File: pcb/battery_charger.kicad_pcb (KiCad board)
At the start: 2 copper layers, 36.2 x 24.2 mm, 20 parts, among them J1 USB_B_Micro, U1 TP4056, U2 DW01A, U3 FS8205A

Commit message: Correcciones generales al pcb
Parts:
- moved C1 0.32 mm to (123.3, 124.8), turned to 0 degrees
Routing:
- net GND: track 97.6 -> 95.7 mm
- net +5V: track 51.4 -> 50.6 mm
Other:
- board text added: "1"
- board text added: "Rev. 1.0"
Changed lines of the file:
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@@
   (general
     (thickness 1.6)
-    (drawings 8)
-    (tracks 145)
+    (drawings 12)
+    (tracks 144)
     (zones 0)
     (modules 20)
@@
   )
   (setup
-    (last_trace_width 0.25)
+    (last_trace_width 0.5)
     (user_trace_width 0.25)
     (user_trace_width 0.5)
@@
   )
   (module Capacitor_SMD:C_0805_2012Metric (layer F.Cu)
-    (at 123.25 125.0625 270)
+    (at 123.3125 124.75)
     (descr "Capacitor SMD 0805 (2012 Metric), square (rectangular) end terminal, IPC_7351 nominal, (Body size source: https://docs.google.com/spreadsheets/d/1BsfQQcO9C6DZCsRaXUlFlo91Tg2WpOkGARC1WS5S8t0/edit?usp=sharing), generated with kicad-footprint-generator")
     (tags capacitor)
     (attr smd)
-    (fp_text reference C1 (at -0.0625 -2 180) (layer F.SilkS)
-      (effects (font (size 1 1) (thickness 0.15)))
-    )
-    (fp_text value 0.1uF (at 0 1.65 90) (layer F.Fab)
-      (effects (font (size 1 1) (thickness 0.15)))
-    )
-    (fp_text user %R (at 0 0 90) (layer F.Fab)
+    (fp_text reference C1 (at 0.1875 -1.75) (layer F.SilkS)
+      (effects (font (size 1 1) (thickness 0.15)))
+    )
+    (fp_text value 0.1uF (at 0 1.65) (layer F.Fab)
+      (effects (font (size 1 1) (thickness 0.15)))
+    )
+    (fp_line (start -1 0.6) (end -1 -0.6) (layer F.Fab) (width 0.1))
+    (fp_line (start -1 -0.6) (end 1 -0.6) (layer F.Fab) (width 0.1))
+    (fp_line (start 1 -0.6) (end 1 0.6) (layer F.Fab) (width 0.1))
+    (fp_line (start 1 0.6) (end -1 0.6) (layer F.Fab) (width 0.1))
+    (fp_line (start -0.258578 -0.71) (end 0.258578 -0.71) (layer F.SilkS) (width 0.12))
+    (fp_line (start -0.258578 0.71) (end 0.258578 0.71) (layer F.SilkS) (width 0.12))
+    (fp_line (start -1.68 0.95) (end -1.68 -0.95) (layer F.CrtYd) (width 0.05))
+    (fp_line (start -1.68 -0.95) (end 1.68 -0.95) (layer F.CrtYd) (width 0.05))
+    (fp_line (start 1.68 -0.95) (end 1.68 0.95) (layer F.CrtYd) (width 0.05))
+    (fp_line (start 1.68 0.95) (end -1.68 0.95) (layer F.CrtYd) (width 0.05))
+    (fp_text user %R (at 0 0) (layer F.Fab)
       (effects (font (size 0.5 0.5) (thickness 0.08)))
     )
-    (fp_line (start 1.68 0.95) (end -1.68 0.95) (layer F.CrtYd) (width 0.05))
-    (fp_line (start 1.68 -0.95) (end 1.68 0.95) (layer F.CrtYd) (width 0.05))
-    (fp_line (start -1.68 -0.95) (end 1.68 -0.95) (layer F.CrtYd) (width 0.05))
-    (fp_line (start -1.68 0.95) (end -1.68 -0.95) (layer F.CrtYd) (width 0.05))
-    (fp_line (start -0.258578 0.71) (end 0.258578 0.71) (layer F.SilkS) (width 0.12))
-    (fp_line (start -0.258578 -0.71) (end 0.258578 -0.71) (layer F.SilkS) (width 0.12))
-    (fp_line (start 1 0.6) (end -1 0.6) (layer F.Fab) (width 0.1))
-    (fp_line (start 1 -0.6) (end 1 0.6) (layer F.Fab) (width 0.1))
-    (fp_line (start -1 -0.6) (end 1 -0.6) (layer F.Fab) (width 0.1))
-    (fp_line (start -1 0.6) (end -1 -0.6) (layer F.Fab) (width 0.1))
-    (pad 2 smd roundrect (at 0.9375 0 270) (size 0.975 1.4) (layers F.Cu F.Paste F.Mask) (roundrect_rratio 0.25)
-      (net 2 GND))
-    (pad 1 smd roundrect (at -0.9375 0 270) (size 0.975 1.4) (layers F.Cu F.Paste F.Mask) (roundrect_rratio 0.25)
+    (pad 1 smd roundrect (at -0.9375 0) (size 0.975 1.4) (layers F.Cu F.Paste F.Mask) (roundrect_rratio 0.25)
       (net 1 +5V))
+    (pad 2 smd roundrect (at 0.9375 0) (size 0.975 1.4) (layers F.Cu F.Paste F.Mask) (roundrect_rratio 0.25)
+      (net 2 GND))
     (model ${KISYS3DMOD}/Capacitor_SMD.3dshapes/C_0805_2012Metric.wrl
       (at (xyz 0 0 0))
@@
     )
   )
-  (dimension 24.25 (width 0.12) (layer F.SilkS)
-    (gr_text "24,250 mm" (at 144.02 129.375 270) (layer F.SilkS)
+  (gr_text 1 (at 129.25 125) (layer F.SilkS)
+    (effects (font (size 0.5 0.5) (thickness 0.125)))
+  )
+  (gr_text 1 (at 130.75 130) (layer F.SilkS)
+    (effects (font (size 0.5 0.5) (thickness 0.125)))
+  )
+  (gr_text "Rev. 1.0" (at 130.5 140.5) (layer F.SilkS)
+    (effects (font (size 0.5 0.5) (thickness 0.1)))
+  )
+  (gr_text 1 (at 113.5 133.25) (layer F.SilkS)
+    (effects (font (size 0.5 0.5) (thickness 0.125)))
+  )
+  (dimension 24.25 (width 0.12) (layer Dwgs.User)
+    (gr_text "24,250 mm" (at 144.02 129.375 270) (layer Dwgs.User)
       (effects (font (size 1 1) (thickness 0.15)))
     )
@@
     (arrow2b (pts (xy 142.75 117.25) (xy 143.336421 118.376504)))
   )
-  (dimension 36.25 (width 0.12) (layer F.SilkS)
-    (gr_text "36,250 mm" (at 120.625 112.48) (layer F.SilkS)
+  (dimension 36.25 (width 0.12) (layer Dwgs.User)
+    (gr_text "36,250 mm" (at 120.625 112.48) (layer Dwgs.User)
       (effects (font (size 1 1) (thickness 0.15)))
     )
@@
     (arrow2b (pts (xy 102.5 113.75) (xy 103.626504 113.163579)))
   )
-  (gr_text "Designed\nin\nArgentina" (at 111 133) (layer F.SilkS)
+  (gr_text "Designed\nin\nArgentina" (at 110.75 133) (layer F.SilkS)
     (effects (font (size 0.7 0.7) (thickness 0.1)))
   )
-  (gr_text "Battery Charger" (at 127 140) (layer F.SilkS)
+  (gr_text "Battery Charger" (at 122.5 139.75) (layer F.SilkS)
     (effects (font (size 1 1) (thickness 0.15)))
   )
@@
   (segment (start 114.595 127.4625) (end 112.210662 127.4625) (width 0.5) (layer F.Cu) (net 1))
   (segment (start 112.173162 127.5) (end 110.75 127.5) (width 0.5) (layer F.Cu) (net 1))
-  (segment (start 122.25 123.125) (end 123.25 124.125) (width 0.5) (layer F.Cu) (net 1))
-  (segment (start 122.25 118) (end 122.25 123.125) (width 0.5) (layer F.Cu) (net 1))
-  (segment (start 119 118) (end 122.25 118) (width 0.5) (layer F.Cu) (net 1))
-  (segment (start 118.5 120.5) (end 118.5 118.5) (width 0.5) (layer F.Cu) (net 1))
-  (segment (start 118.5 118.5) (end 119 118) (width 0.5) (layer F.Cu) (net 1))
   (segment (start 113.1875 120.5) (end 113.1875 118.3125) (width 0.5) (layer F.Cu) (net 1))
   (segment (start 110.6875 118.3125) (end 108.75 120.25) (width 0.5) (layer F.Cu) (net 1))
@@
   (segment (start 110.75 127.5) (end 109.375 126.125) (width 0.5) (layer F.Cu) (net 1))
   (segment (start 109.375 126.125) (end 108.75 125.5) (width 0.5) (layer F.Cu) (net 1))
+  (segment (start 118.5 120.5) (end 118.5 118.5) (width 0.5) (layer F.Cu) (net 1))
+  (segment (start 118.5 118.5) (end 118.75 118.25) (width 0.5) (layer F.Cu) (net 1))
+  (segment (start 118.75 118.25) (end 121 118.25) (width 0.5) (layer F.Cu) (net 1))
+  (segment (start 122.375 119.625) (end 122.375 124.75) (width 0.5) (layer F.Cu) (net 1))
+  (segment (start 121 118.25) (end 122.375 119.625) (width 0.5) (layer F.Cu) (net 1))
   (segment (start 117.135 135.76) (end 117.135 132.5375) (width 0.5) (layer F.Cu) (net 2))
   (segment (start 118.875 137.5) (end 117.135 135.76) (width 0.5) (layer F.Cu) (net 2))
@@
   (segment (start 130.400002 139.375) (end 131.275002 138.5) (width 0.5) (layer F.Cu) (net 2))
   (segment (start 128.825 130.05) (end 128.825 129.074998) (width 0.25) (layer F.Cu) (net 2))
-  (segment (start 128.825 129.074998) (end 128.949999 128.949999) (width 0.25) (layer F.Cu) (net 2))
   (via (at 132.25 134.75) (size 0.8) (drill 0.4) (layers F.Cu B.Cu) (net 2))
   (segment (start 130.699999 128.949999) (end 132.25 130.5) (width 0.25) (layer F.Cu) (net 2))
@@
   (segment (start 128.949999 128.949999) (end 129.300001 128.949999) (width 0.25) (layer F.Cu) (net 2))
   (segment (start 129.300001 128.949999) (end 130.699999 128.949999) (width 0.25) (layer F.Cu) (net 2))
-  (segment (start 125.25 124) (end 125.25 120.5) (width 0.5) (layer F.Cu) (net 2))
-  (segment (start 123.25 126) (end 125.25 124) (width 0.5) (layer F.Cu) (net 2))
   (segment (start 126.5 119.25) (end 125.25 120.5) (width 0.25) (layer F.Cu) (net 2))
   (segment (start 132 119.25) (end 126.5 119.25) (width 0.25) (layer F.Cu) (net 2))
@@
   (segment (start 108.75 135.8) (end 110.2 137.25) (width 0.25) (layer F.Cu) (net 2))
   (segment (start 108.75 132.314998) (end 108.75 135.8) (width 0.25) (layer F.Cu) (net 2))
+  (segment (start 124.25 124.75) (end 125.25 123.75) (width 0.5) (layer F.Cu) (net 2))
+  (segment (start 125.25 123.75) (end 125.25 120.5) (width 0.5) (layer F.Cu) (net 2))
   (segment (start 124.625 129.45) (end 124.625 130.25) (width 0.5) (layer F.Cu) (net 3))
   (segment (start 124.625 128.53) (end 124.625 129.45) (width 0.5) (layer F.Cu) (net 3))

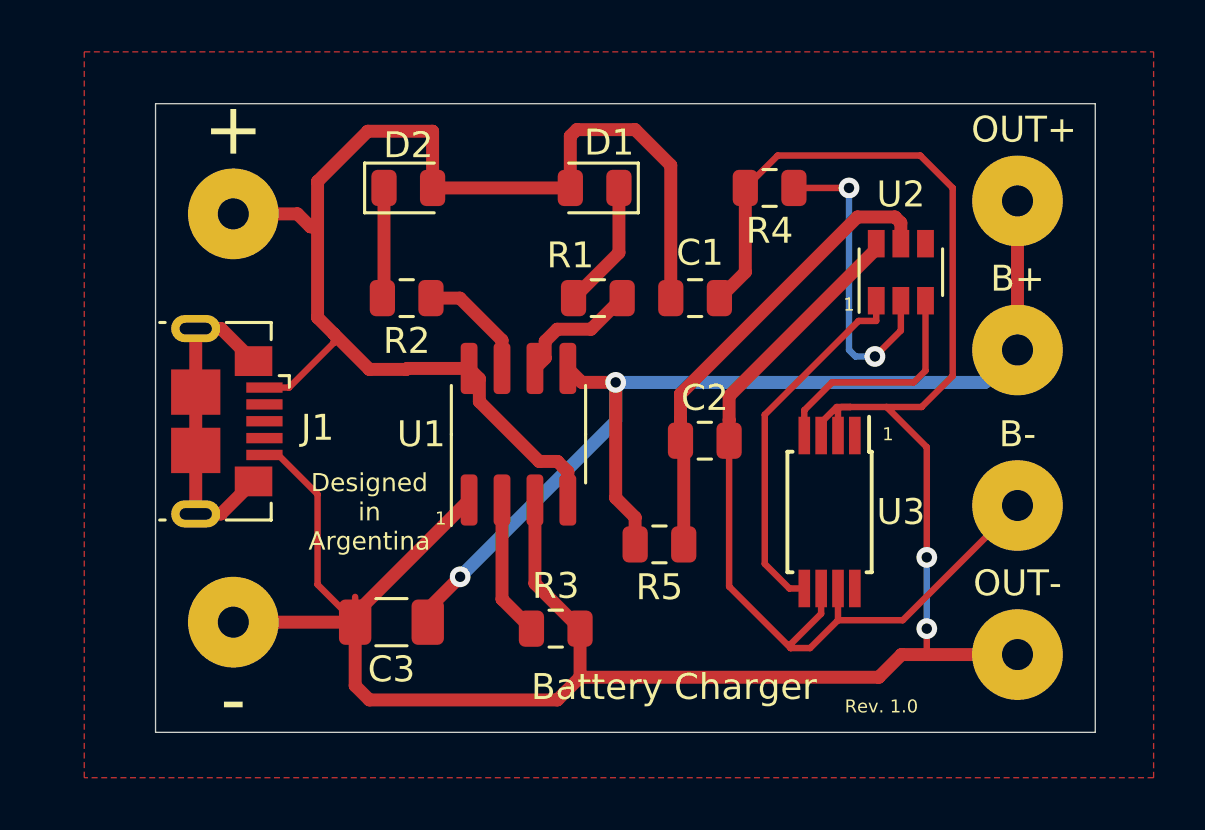
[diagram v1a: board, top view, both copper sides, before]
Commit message: Correcciones a esquematico
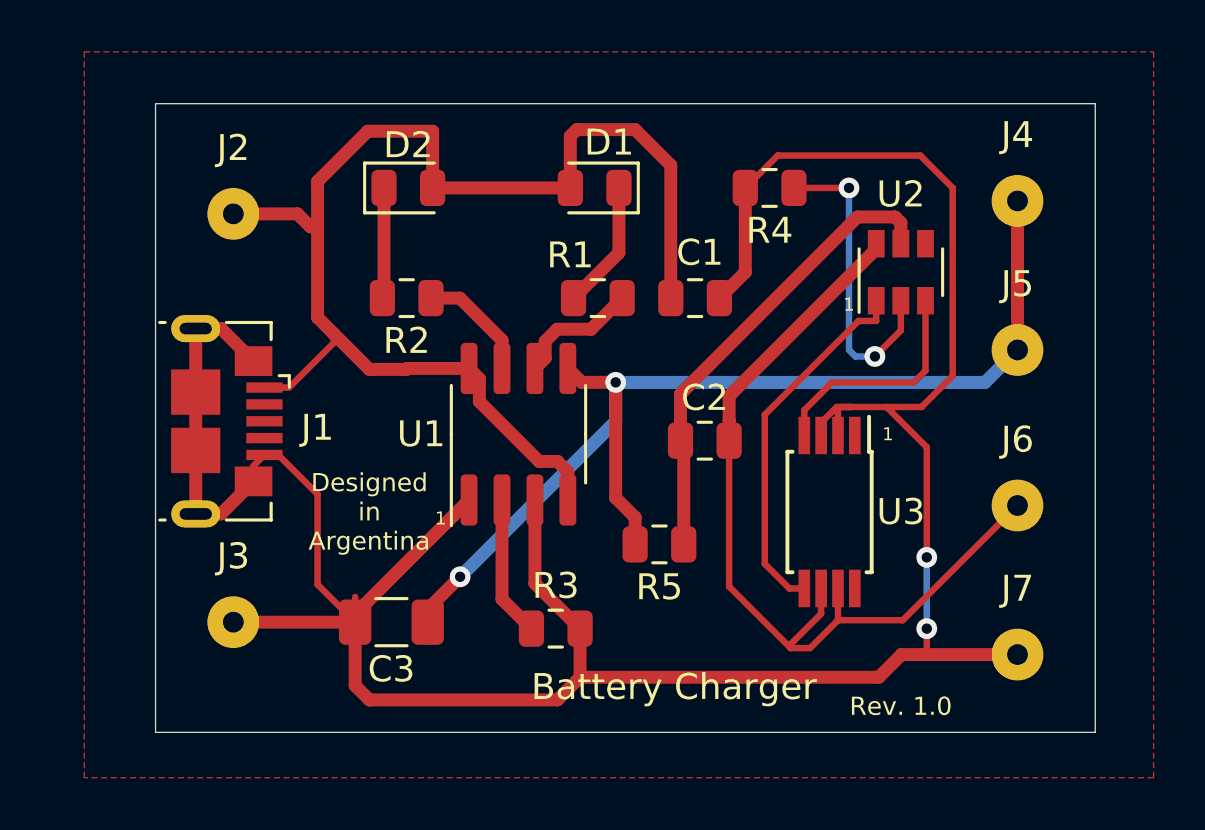
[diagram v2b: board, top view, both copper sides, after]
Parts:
- J2: renamed from +; footprint Connector_Wire:SolderWirePad_1x01_Drill1.2mm -> Connector_Wire:SolderWirePad_1x01_Drill0.8mm
- J3: renamed from -; footprint Connector_Wire:SolderWirePad_1x01_Drill1.2mm -> Connector_Wire:SolderWirePad_1x01_Drill0.8mm
- J4: renamed from OUT+; footprint Connector_Wire:SolderWirePad_1x01_Drill1.2mm -> Connector_Wire:SolderWirePad_1x01_Drill0.8mm
- J5: renamed from B+; footprint Connector_Wire:SolderWirePad_1x01_Drill1.2mm -> Connector_Wire:SolderWirePad_1x01_Drill0.8mm
- J6: renamed from B-; footprint Connector_Wire:SolderWirePad_1x01_Drill1.2mm -> Connector_Wire:SolderWirePad_1x01_Drill0.8mm
- J7: renamed from OUT-; footprint Connector_Wire:SolderWirePad_1x01_Drill1.2mm -> Connector_Wire:SolderWirePad_1x01_Drill0.8mm
- R5: value 0.1K -> 100R
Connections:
- J1 pad 6: Net-(J1-Pad6) -> GND
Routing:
- net GND: track 95.7 -> 109.6 mm
- net Net-(J1-Pad6): track 12.6 -> 0.00 mm

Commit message: Importantes mejoras en el PCB
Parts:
- removed J2: IN+, Connector_Wire:SolderWirePad_1x01_Drill0.8mm
- removed J7: OUT-, Connector_Wire:SolderWirePad_1x01_Drill0.8mm
- added +: IN+, Connector_Wire:SolderWirePad_1x01_Drill0.8mm, F.Cu at (105.2, 123.0)
- added OUT-: OUT-, Connector_Wire:SolderWirePad_1x01_Drill0.8mm, F.Cu at (129.0, 135.5)
- moved C3 19.9 mm to (126.0, 123.5), turned to 270 degrees
- moved U2 13.8 mm to (119.0, 130.0), turned to 270 degrees
- moved OUT+ 7.12 mm to (129.0, 123.2)
- moved B- 6.86 mm to (129.0, 131.5)
- moved B+ 6.77 mm to (129.0, 127.2)
- moved C2 5.76 mm to (124.0, 136.0)
- moved U3 4.85 mm to (124.5, 130.2)
- moved U1 4.25 mm to (112.2, 130.0)
- moved R4 3.91 mm to (122.7, 122.2)
- moved D1 3.00 mm to (117.0, 122.2)
- moved R5 2.61 mm to (120.0, 136.0)
- moved C1 2.56 mm to (120.8, 124.8)
- moved R1 2.56 mm to (117.0, 124.8)
- moved R3 2.40 mm to (116.1, 136.0)
- moved D2 2.02 mm to (111.2, 122.2)
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- renumbered J3 to -, J5 to B+, J6 to B-, J4 to OUT+
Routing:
- net GND: track 109.6 -> 11.4 mm, vias 2 -> 0
- net Net-(C2-Pad2): track 34.0 -> 18.7 mm
- net Net-(C2-Pad1): track 18.1 -> 7.83 mm
- net +5V: track 50.6 -> 41.2 mm
- net Net-(C3-Pad1): track 42.6 -> 33.3 mm, vias 2 -> 1
- net Net-(U2-Pad1): track 14.2 -> 6.48 mm
- net Net-(R4-Pad1): track 12.0 -> 9.38 mm, vias 2 -> 0
- net Net-(R1-Pad2): track 4.87 -> 6.88 mm
- net Net-(D2-Pad1): track 4.28 -> 2.50 mm
- net Net-(D1-Pad1): track 4.97 -> 3.38 mm
- net Net-(R2-Pad1): track 4.50 -> 2.95 mm
- net Net-(U2-Pad3): track 8.98 -> 9.19 mm, vias 0 -> 2
- added copper zone on B.Cu, net GND
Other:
- board size 36.2 x 24.2 mm -> 29 x 18.5 mm
- net class Default: clearance 0.25 -> 0.3
- rule trace_clearance: 0.25 -> 0.3
- board text added: "Cargador Batería"
- board text added: "Grilla componentes: 0.5mm - 0.25mm Grilla pistas: 0.25mm Vías: 1mm Pistas: 0.75mm - 0.5mm - 0.25mm Clearance: 0.3mm (0.2mm para U3) FR4 - 1.6mm espesor Terminación HASL"
- board text added: "Ind. Arg."
- board text added: "Rev. 1"
- board text removed: "Battery Charger"
- board text removed: "Designed in Argentina"
- board text removed: "Rev. 1.0"

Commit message: Se agregan referencias del fabricante
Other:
- board text added: "Grilla componentes: 0.5mm - 0.25mm Grilla pistas: 0.25mm Vías: 1mm (Límite Mayer 8mils - 0.80mm) Pistas: 0.75mm - 0.5mm - 0.25mm (Límite Mayer 8mils - 0.20mm) Clearance: 0.3mm - 0.2mm para U3 (Límite Mayer 8mils - 0.18mm) FR4 - 1.6mm espesor Terminación HASL"
- board text removed: "Grilla componentes: 0.5mm - 0.25mm Grilla pistas: 0.25mm Vías: 1mm Pistas: 0.75mm - 0.5mm - 0.25mm Clearance: 0.3mm (0.2mm para U3) FR4 - 1.6mm espesor Terminación HASL"
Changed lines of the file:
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@@
   )
   (setup
-    (last_trace_width 0.5)
+    (last_trace_width 0.25)
     (user_trace_width 0.25)
     (user_trace_width 0.5)
@@
     (effects (font (size 0.5 0.5) (thickness 0.125)))
   )
-  (gr_text "Grilla componentes: 0.5mm - 0.25mm\nGrilla pistas: 0.25mm\nVías: 1mm\nPistas: 0.75mm - 0.5mm - 0.25mm\nClearance: 0.3mm (0.2mm para U3)\n\nFR4 - 1.6mm espesor\nTerminación HASL" (at 142.5 128.25) (layer Dwgs.User)
+  (gr_text "Grilla componentes: 0.5mm - 0.25mm\nGrilla pistas: 0.25mm\nVías: 1mm (Límite Mayer 8mils - 0.80mm)\nPistas: 0.75mm - 0.5mm - 0.25mm (Límite Mayer 8mils - 0.20mm)\nClearance: 0.3mm - 0.2mm para U3 (Límite Mayer 8mils - 0.18mm)\n\nFR4 - 1.6mm espesor\nTerminación HASL" (at 142.5 128.25) (layer Dwgs.User)
     (effects (font (size 1 1) (thickness 0.15)) (justify left))
   )
